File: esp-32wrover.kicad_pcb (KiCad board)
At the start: 2 copper layers, 68.6 x 53.3 mm, 79 parts, among them CON1 BARREL_JACK, P1 Power, P10 ICSP, P2 Analog, P3 Digital, P4 Digital, P5 CONN_1, P6 CONN_1, P7 CONN_1, P8 CONN_1, P9 CONN_01X04, Q3 Q_NPN_BEC, Q4 Q_NPN_BEC, SW1 SW_PUSH, SW2 SW_PUSH, U1 usb_mini_b, U2 MCP16311-MNY, U3 BD00GA5WEFJ, U4 PL2303HXA, U5 MCP6001R, U6 ESP32-WROVER, U7 IRLM6402, Y1 12Mhz, Y2 32.768Khz

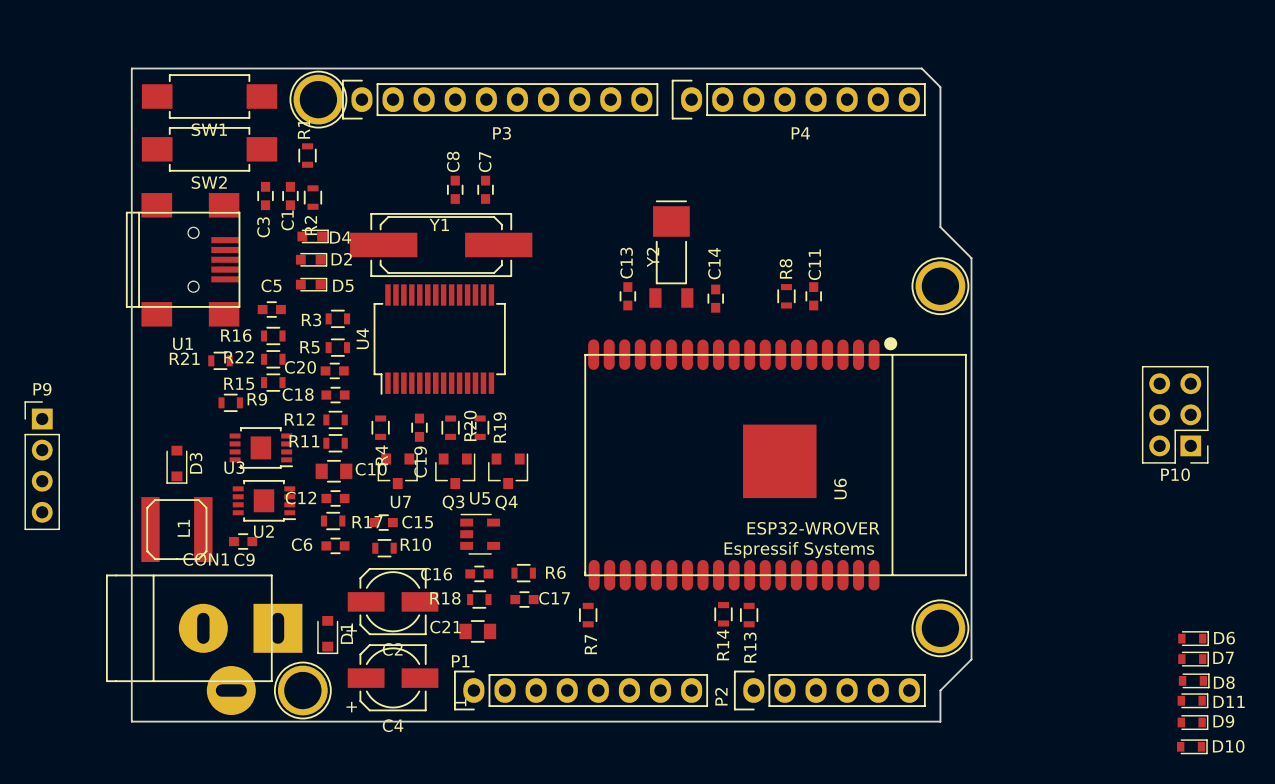
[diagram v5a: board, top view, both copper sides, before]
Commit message: sắp xếp linh kiện, đi dây
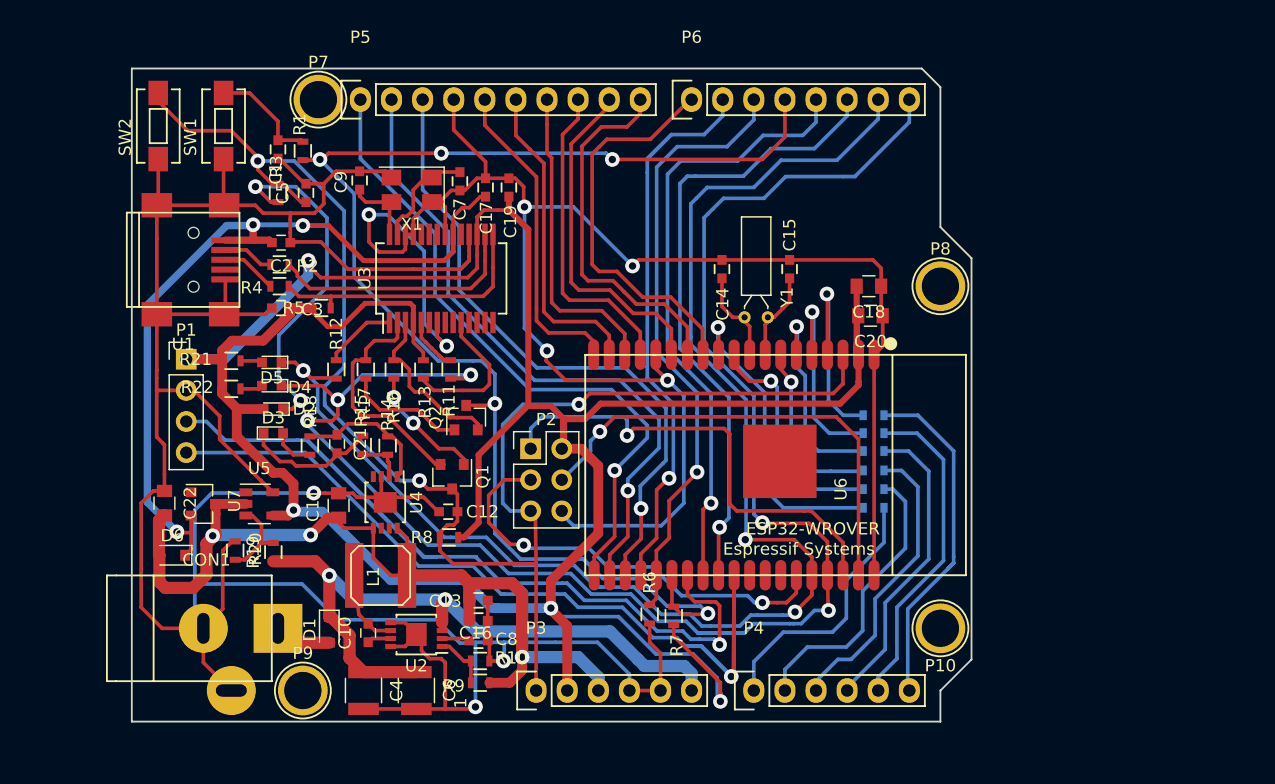
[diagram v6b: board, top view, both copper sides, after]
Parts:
- removed Q3, Q4: Q_NPN_BEC, TO_SOT_Packages_SMD:SOT-23
- removed Y2: 32.768Khz, Crystals:Crystal_SMD_Micro-Crystal_MS1V-T1K
- added C22: 100nF, Capacitors_SMD:C_0805, F.Cu at (113.7, 108.5)
- added D12: ZENER_3.3V, Diodes_SMD:D_0603, B.Cu at (171.6, 104.3)
- added Q1: Q_NPN_BEC, TO_SOT_Packages_SMD:SOT-23, F.Cu at (137.2, 106.4)
- added Q2: Q_NPN_BEC, TO_SOT_Packages_SMD:SOT-23, F.Cu at (138.3, 101.5)
- added X1: CRYSTAL_ABM3C, Crystals:Crystal_SMD_5032-4pin_5.0x3.2mm, F.Cu at (133.9, 82.9)
- C10: value 1uF -> 100nF; footprint Capacitors_SMD:C_0805 -> Capacitors_SMD:C_0603
- C11: value C -> 1uF; footprint Capacitors_SMD:C_0603 -> Capacitors_SMD:C_0805
- C12, C15: value 10uF/25V -> C
- C13, C16: value C -> 10uF/25V
- C17: value C -> 0.1uF
- C18: value 1uF/25V -> C; footprint Capacitors_SMD:C_0603 -> Capacitors_SMD:C_0805
- C2: value 10uF/25V -> 10uF; footprint Capacitors_SMD:c_elec_5x5.3 -> Capacitors_SMD:C_0603
- C20: value 0.1uF -> C; footprint Capacitors_SMD:C_0603 -> Capacitors_SMD:C_0805
- C21: value 100nF -> 1uF/25V; footprint Capacitors_SMD:C_0805 -> Capacitors_SMD:C_0603
- C3: value 1nF/50V -> 33pF
- C4: footprint Capacitors_SMD:c_elec_5x5.3 -> Capacitors_SMD:C_1210
- C5: value 10uF -> 1nF/50V
- C6: value 1uF -> 10uF/25V; footprint Capacitors_SMD:C_0603 -> Capacitors_SMD:C_1210
- C8: value 33pF -> 1uF
- C9: value 100nF -> 33pF
- D10, D11, D7, D8, D9: moved to B.Cu
- D2: value L_PWR -> L-RST
- D3: value SS24 -> L_PWR; footprint Diodes_SMD:D_0805 -> LEDs:LED_0603
- D6: value ZENER_3.3V -> SS24; footprint Diodes_SMD:D_0603 -> Diodes_SMD:D_0805
- P1: value Power -> CONN_01X04; footprint Socket_Arduino_Uno:Socket_Strip_Arduino_1x08 -> Pin_Headers:Pin_Header_Straight_1x04_Pitch2.54mm
- P10: value ICSP -> CONN_1; footprint Pin_Headers:Pin_Header_Straight_2x03_Pitch2.54mm -> new:Arduino_1pin
- P2: value Analog -> ICSP; footprint Socket_Arduino_Uno:Socket_Strip_Arduino_1x06 -> Pin_Headers:Pin_Header_Straight_2x03_Pitch2.54mm
- P3: value Digital -> Analog; footprint Socket_Arduino_Uno:Socket_Strip_Arduino_1x10 -> new:Socket_Strip_Arduino_1x06
- P4: value Digital -> Analog; footprint Socket_Arduino_Uno:Socket_Strip_Arduino_1x08 -> new:Socket_Strip_Arduino_1x06
- P5: value CONN_1 -> Digital; footprint Socket_Arduino_Uno:Arduino_1pin -> new:Socket_Strip_Arduino_1x10
- P6: value CONN_1 -> Digital; footprint Socket_Arduino_Uno:Arduino_1pin -> new:Socket_Strip_Arduino_1x08
- P7, P8: footprint Socket_Arduino_Uno:Arduino_1pin -> new:Arduino_1pin
- P9: value CONN_01X04 -> CONN_1; footprint Pin_Headers:Pin_Header_Straight_1x04_Pitch2.54mm -> new:Arduino_1pin
- R11: value 3K -> 470R
- R12: value 1K -> 470R
- R13: value 470R -> 4K7
- R14: value 470R -> 3K
- R15: value 4K7 -> 1K
- R16: value 470R -> 1K
- R17: value 10K -> 1K
- R18: value 10K -> 470R
- R19, R20: value 1K -> 10K
- R2: value 470R -> 27R
- R3: value 27R -> 470R
- SW1, SW2: footprint Buttons_Switches_SMD:SW_SPST_REED_CT05-XXXX-G1 -> Buttons_Switches_SMD:SW_SPST_EVQPE1
- U3: value BD00GA5WEFJ -> PL2303HXA; footprint Housings_SSOP:MSOP-8-1EP_3x3mm_Pitch0.65mm -> Housings_SSOP:SSOP-28_5.3x10.2mm_Pitch0.65mm
- U4: value PL2303HXA -> BD00GA5WEFJ; footprint Housings_SSOP:SSOP-28_5.3x10.2mm_Pitch0.65mm -> Housings_SSOP:MSOP-8-1EP_3x3mm_Pitch0.65mm
- U6: footprint thu-vien:esp32-wrover -> new:esp32-wrover
- Y1: value 12Mhz -> 32.768Khz; footprint Crystals:Q_49U3HMS -> Crystals:Crystal_DS26_d2.0mm_l6.0mm_Horizontal
- moved D6 83.6 mm to (114.3, 112.8)
- moved P3 50.3 mm to (144.0, 123.8)
- moved P4 48.5 mm to (161.8, 123.8)
- moved P5 48.5 mm to (129.7, 75.6)
- moved P6 47.7 mm to (156.7, 75.6)
- moved C18 44.5 mm to (171.2, 90.8)
- moved C20 44.0 mm to (171.3, 93.2)
- moved C11 42.4 mm to (127.9, 108.7)
- moved C15 39.1 mm to (164.7, 89.4), turned to 90 degrees
- moved C8 36.9 mm to (139.3, 119.8), turned to 0 degrees
- moved D10 36.5 mm to (171.6, 102.8)
- moved P1 35.8 mm to (115.4, 96.8)
- moved D11 34.9 mm to (171.6, 101.3)
- moved R8 33.9 mm to (136.9, 111.3), turned to 180 degrees
- moved C17 33.8 mm to (139.9, 82.7), turned to 270 degrees
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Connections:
- C10 pad 1: +5V -> Net-(C10-Pad1)
- C10 pad 2: GND -> Net-(C10-Pad2)
- C11 pad 1: GND -> +5V
- C11 pad 2: EN -> GND
- C12 pad 1: +5V -> GND
- C12 pad 2: GND -> EN
- C13 pad 1: Net-(C13-Pad1) -> +5V
- C15 pad 1: +5V -> Net-(C15-Pad1)
- C16 pad 1: GND -> +5V
- C16 pad 2: +3V3 -> GND
- C17 pad 2: +3V3 -> VCC
- C18 pad 1: Net-(C18-Pad1) -> GND
- C18 pad 2: Net-(C18-Pad2) -> +3V3
- C19 pad 2: VCC -> +3V3
- C2 pad 1: Vin -> GND
- C2 pad 2: GND -> VCC
- C21 pad 1: GND -> Net-(C21-Pad1)
- C21 pad 2: +5V -> Net-(C21-Pad2)
- C3 pad 1: Net-(C3-Pad1) -> GND
- C3 pad 2: GND -> +3V3
- C5 pad 1: GND -> EN
- C5 pad 2: VCC -> GND
- C6 pad 1: Net-(C6-Pad1) -> Vin
- C9 pad 2: Net-(C9-Pad2) -> GND
- D10 pad 1: A5 -> A4
- D10 pad 2: ADC-5 -> ADC-4
- D11 pad 1: A3 -> A5
- D11 pad 2: ADC-3 -> ADC-5
- D2 pad 1: Net-(C18-Pad2) -> Net-(D2-Pad1)
- D2 pad 2: Net-(D2-Pad2) -> +3V3
- D3 pad 1: VCC -> Net-(C21-Pad2)
- D3 pad 2: +5V -> Net-(D3-Pad2)
- D6 pad 1: A0 -> VCC
- D6 pad 2: ADC-0 -> +5V
- D7 pad 1: A1 -> A0
- D7 pad 2: ADC-1 -> ADC-0
- D8 pad 1: A2 -> A1
- D8 pad 2: ADC-2 -> ADC-1
- D9 pad 1: A4 -> A2
- D9 pad 2: ADC-4 -> ADC-2
- L1 pad 1: Net-(C9-Pad2) -> Net-(C10-Pad2)
- P1 pad 1: (no net) -> +3V3
- P1 pad 2: (no net) -> GND
- P1 pad 3: EN -> SCL
- P1 pad 4: +3V3 -> SDA
- P10 pad 1: IO22 -> (no net)
- P2 pad 1: A0 -> IO22
- P2 pad 2: A1 -> +3V3
- P2 pad 3: A2 -> IO21
- P2 pad 4: A3 -> IO23
- P2 pad 5: A4 -> EN
- P2 pad 6: A5 -> GND
- P3 pad 1: SD1 -> EN
- P3 pad 2: SDO -> +3V3
- P3 pad 3: CLK -> +5V
- P3 pad 5: CMD -> GND
- P3 pad 6: SD3 -> Vin
- P4 pad 1: IO27 -> A0
- P4 pad 2: IO15 -> A1
- P4 pad 3: GPIO2 -> A2
- P4 pad 4: GPIO0 -> A3
- P4 pad 5: IO16 -> A4
- P4 pad 6: IO17 -> A5
- P5 pad 1: (no net) -> CLK
- P6 pad 1: (no net) -> IO27
- P9 pad 1: +3V3 -> (no net)
- R11 pad 1: Net-(C18-Pad1) -> Net-(R11-Pad1)
- R11 pad 2: Net-(R11-Pad2) -> RXD
- R12 pad 1: Net-(R11-Pad2) -> Net-(R12-Pad1)
- R12 pad 2: Net-(C18-Pad2) -> TXD
- R13 pad 2: RXD -> +3V3
- R14 pad 1: Net-(R14-Pad1) -> Net-(C21-Pad1)
- R14 pad 2: TXD -> Net-(R14-Pad2)
- R15 pad 1: Net-(R15-Pad1) -> Net-(R14-Pad2)
- R15 pad 2: +3V3 -> Net-(C21-Pad2)
- R16 pad 1: Net-(C18-Pad1) -> Net-(Q2-Pad2)
- R16 pad 2: Net-(D2-Pad2) -> Net-(Q1-Pad1)
- R17 pad 1: Vin -> Net-(Q1-Pad2)
- R17 pad 2: Net-(R17-Pad2) -> Net-(Q2-Pad1)
- R18 pad 1: Net-(R17-Pad2) -> Net-(C21-Pad1)
- R18 pad 2: GND -> Net-(D3-Pad2)
- R19 pad 1: Net-(Q4-Pad2) -> Vin
- R19 pad 2: Net-(Q3-Pad1) -> Net-(R19-Pad2)
- R2 pad 1: EN -> Net-(R2-Pad1)
- R2 pad 2: Net-(C3-Pad1) -> Net-(R2-Pad2)
- R20 pad 1: Net-(Q3-Pad2) -> Net-(R19-Pad2)
- R20 pad 2: Net-(Q4-Pad1) -> GND
- R3 pad 1: Net-(R3-Pad1) -> Net-(D2-Pad1)
- R3 pad 2: Net-(R3-Pad2) -> EN
- SW2 pad 2: Net-(C3-Pad1) -> EN
- U1 pad 2: Net-(R3-Pad2) -> Net-(R2-Pad2)
- U2 pad 2: Net-(C6-Pad1) -> Net-(C8-Pad1)
- U2 pad 6: Net-(C9-Pad2) -> Net-(C10-Pad2)
- U2 pad 7: Net-(C9-Pad1) -> Net-(C10-Pad1)
- U3 pad 1: Net-(C18-Pad1) -> Net-(R12-Pad1)
- U3 pad 2: Net-(R11-Pad2) -> Net-(Q1-Pad2)
- U3 pad 3: GND -> Net-(Q2-Pad2)
- U3 pad 4: (no net) -> +3V3
- U3 pad 5: +5V -> Net-(R11-Pad1)
- U3 pad 7: (no net) -> GND
- U3 pad 8: +5V -> (no net)
- U3 pad 9: GND -> (no net)
- U4 pad 1: Net-(R14-Pad1) -> Net-(C21-Pad1)
- U4 pad 2: Net-(Q3-Pad2) -> Net-(R14-Pad2)
- U4 pad 3: Net-(Q4-Pad2) -> GND
- U4 pad 4: +3V3 -> (no net)
- U4 pad 5: Net-(R13-Pad1) -> +5V
- U4 pad 7: GND -> (no net)
- U4 pad 8: (no net) -> +5V
- U4 pad 9: (no net) -> GND
- U5 pad 3: Net-(R17-Pad2) -> Net-(R19-Pad2)
- U6 pad 10: ADC-4 -> ADC-1
- U6 pad 11: ADC-5 -> ADC-0
- U6 pad 4: ADC-0 -> ADC-5
- U6 pad 5: ADC-1 -> ADC-4
- U6 pad 6: ADC-2 -> ADC-3
- U6 pad 7: ADC-3 -> ADC-2
- U6 pad 8: Net-(C14-Pad1) -> Net-(C15-Pad1)
- U6 pad 9: Net-(C13-Pad1) -> Net-(C14-Pad1)
- Y1 pad 1: Net-(C8-Pad1) -> Net-(C15-Pad1)
- Y1 pad 2: Net-(C7-Pad1) -> Net-(C14-Pad1)
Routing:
- net GND: track 0.00 -> 412.6 mm, vias 0 -> 9
- net +3V3: track 0.00 -> 253.1 mm, vias 0 -> 4
- net RXD: track 0.00 -> 137.6 mm, vias 0 -> 5
- net EN: track 0.00 -> 127.2 mm, vias 0 -> 3
- net TXD: track 0.00 -> 115.7 mm, vias 0 -> 3
- net GPIO0: track 0.00 -> 110.4 mm, vias 0 -> 5
- net +5V: track 0.00 -> 79.3 mm, vias 0 -> 3
- net SDA: track 0.00 -> 73.6 mm, vias 0 -> 1
- net SCL: track 0.00 -> 73.4 mm, vias 0 -> 1
- net VCC: track 0.00 -> 67.5 mm, vias 0 -> 3
- net Vin: track 0.00 -> 56.4 mm, vias 0 -> 2
- net CLK: track 0.00 -> 54.3 mm, vias 0 -> 1
- net SDO: track 0.00 -> 53.7 mm, vias 0 -> 1
- net SD1: track 0.00 -> 52.7 mm, vias 0 -> 1
- net IO17: track 0.00 -> 51.3 mm, vias 0 -> 1
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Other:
- net class Default: trace_width 0.25 -> 0.3; via_dia 1 -> 1.2; via_drill 0.5 -> 0.6
- net class add: trace_width 0.6 -> 1
